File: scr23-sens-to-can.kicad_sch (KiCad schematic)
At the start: 67 parts, among them J1 ATM13-12PA-BM01, U1 LDL1117S50R, U2 LM358_DFN, U3 LM358_DFN, U4 TJA1042T-3, U5 AP7370-33Y-13, U6 LM358_DFN, U7 LM358_DFN, U8 STM32G431CBT6, Y1 Crystal 4-48MHz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

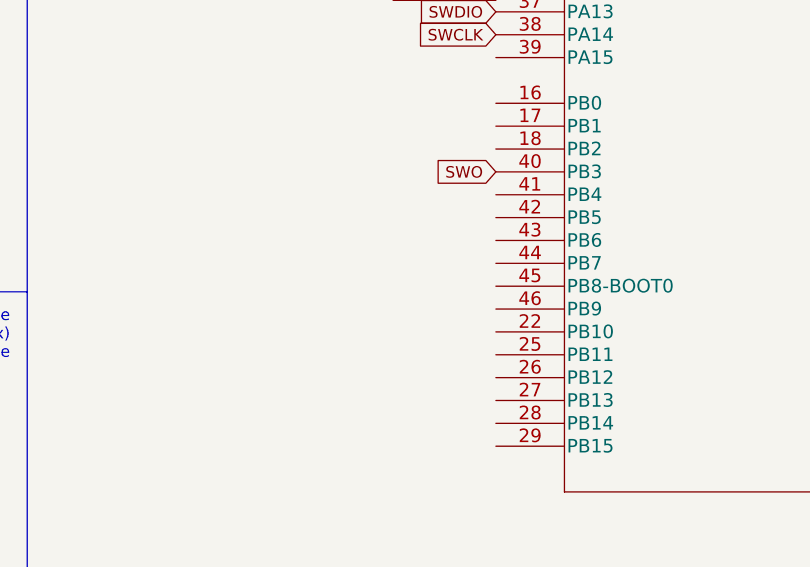
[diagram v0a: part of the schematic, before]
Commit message: added boot0 spdt
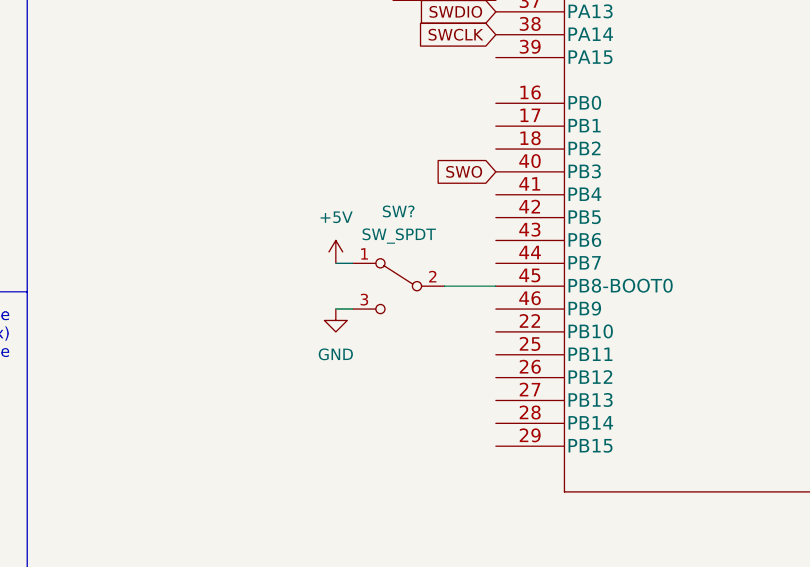
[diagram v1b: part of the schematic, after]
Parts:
- added SW?: SW_SPDT, symbol Switch:SW_SPDT
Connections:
- net +5V: now also SW?.1 (A)
- net GND: now also SW?.3 (C)
- net at U8.45 (PB8-BOOT0): now also SW?.2 (B)
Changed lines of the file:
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@@
     (stroke (width 0) (type default) (color 0 0 0 0))
   )
+  (wire (pts (xy 256.54 97.79) (xy 262.255 97.79))
+    (stroke (width 0) (type default) (color 0 0 0 0))
+  )
   (wire (pts (xy 364.49 39.37) (xy 364.49 36.195))
     (stroke (width 0) (type default) (color 0 0 0 0))
@@
     (stroke (width 0) (type default) (color 0 0 0 0))
   )
+  (wire (pts (xy 244.475 95.25) (xy 246.38 95.25))
+    (stroke (width 0) (type default) (color 0 0 0 0))
+  )
   (wire (pts (xy 57.785 127.635) (xy 54.61 127.635))
     (stroke (width 0) (type default) (color 0 0 0 0))
@@
     (stroke (width 0) (type default) (color 0 0 0 0))
   )
+  (wire (pts (xy 244.475 100.33) (xy 246.38 100.33))
+    (stroke (width 0) (type default) (color 0 0 0 0))
+  )
   (wire (pts (xy 154.94 39.37) (xy 165.1 39.37))
     (stroke (width 0) (type default) (color 0 0 0 0))
@@
     (pin "1")
   )
+  (symbol (lib_id "Switch:SW_SPDT") (at 251.46 97.79 0) (mirror y) (unit 1)
+    (in_bom yes) (on_board yes) (fields_autoplaced)
+    (property "Reference" "SW?" (id 0) (at 251.46 89.535 0))
+    (property "Value" "SW_SPDT" (id 1) (at 251.46 92.075 0))
+    (property "Footprint" "" (id 2) (at 251.46 97.79 0)
+      (effects (font (size 1.27 1.27)) hide)
+    )
+    (property "Datasheet" "~" (id 3) (at 251.46 97.79 0)
+      (effects (font (size 1.27 1.27)) hide)
+    )
+    (pin "1")
+    (pin "2")
+    (pin "3")
+  )
   (symbol (lib_id "Amplifier_Operational:LM358_DFN") (at 186.69 169.545 0) (unit 1)
     (in_bom yes) (on_board yes) (fields_autoplaced)
@@
     (pin "2")
   )
+  (symbol (lib_id "power:+5V") (at 244.475 95.25 0) (unit 1)
+    (in_bom yes) (on_board yes) (fields_autoplaced)
+    (property "Reference" "#PWR?" (id 0) (at 244.475 99.06 0)
+      (effects (font (size 1.27 1.27)) hide)
+    )
+    (property "Value" "+5V" (id 1) (at 244.475 90.17 0))
+    (property "Footprint" "" (id 2) (at 244.475 95.25 0)
+      (effects (font (size 1.27 1.27)) hide)
+    )
+    (property "Datasheet" "" (id 3) (at 244.475 95.25 0)
+      (effects (font (size 1.27 1.27)) hide)
+    )
+    (pin "1")
+  )
   (symbol (lib_id "scr23-sens-to-can-main:LDL1117S50R") (at 127.635 74.93 0) (unit 1)
     (in_bom yes) (on_board yes) (fields_autoplaced)
@@
     (pin "1")
   )
+  (symbol (lib_id "power:GND") (at 244.475 100.33 0) (unit 1)
+    (in_bom yes) (on_board yes) (fields_autoplaced)
+    (property "Reference" "#PWR?" (id 0) (at 244.475 106.68 0)
+      (effects (font (size 1.27 1.27)) hide)
+    )
+    (property "Value" "GND" (id 1) (at 244.475 105.41 0))
+    (property "Footprint" "" (id 2) (at 244.475 100.33 0)
+      (effects (font (size 1.27 1.27)) hide)
+    )
+    (property "Datasheet" "" (id 3) (at 244.475 100.33 0)
+      (effects (font (size 1.27 1.27)) hide)
+    )
+    (pin "1")
+  )
   (symbol (lib_id "power:+3.3V") (at 114.3 122.555 0) (unit 1)
     (in_bom yes) (on_board yes) (fields_autoplaced)
@@
       (reference "#PWR050") (unit 1) (value "GND") (footprint "")
     )
+    (path "/b2bb01a9-b60a-4528-aafa-2c7963462d4c"
+      (reference "#PWR?") (unit 1) (value "+5V") (footprint "")
+    )
+    (path "/cf8dda6e-a56a-43d8-94fc-1ec0cec4f2bf"
+      (reference "#PWR?") (unit 1) (value "GND") (footprint "")
+    )
     (path "/d8e70cec-745e-46da-bcc4-460dc4f54f47"
       (reference "C1") (unit 1) (value "10uF") (footprint "")
@@
       (reference "R18") (unit 1) (value "2670") (footprint "")
     )
+    (path "/098c6e6c-eb58-4a2a-b1cd-84ff9a7d7a07"
+      (reference "SW?") (unit 1) (value "SW_SPDT") (footprint "")
+    )
     (path "/b44bb0d9-577b-4e0b-a8dd-da899da62349"

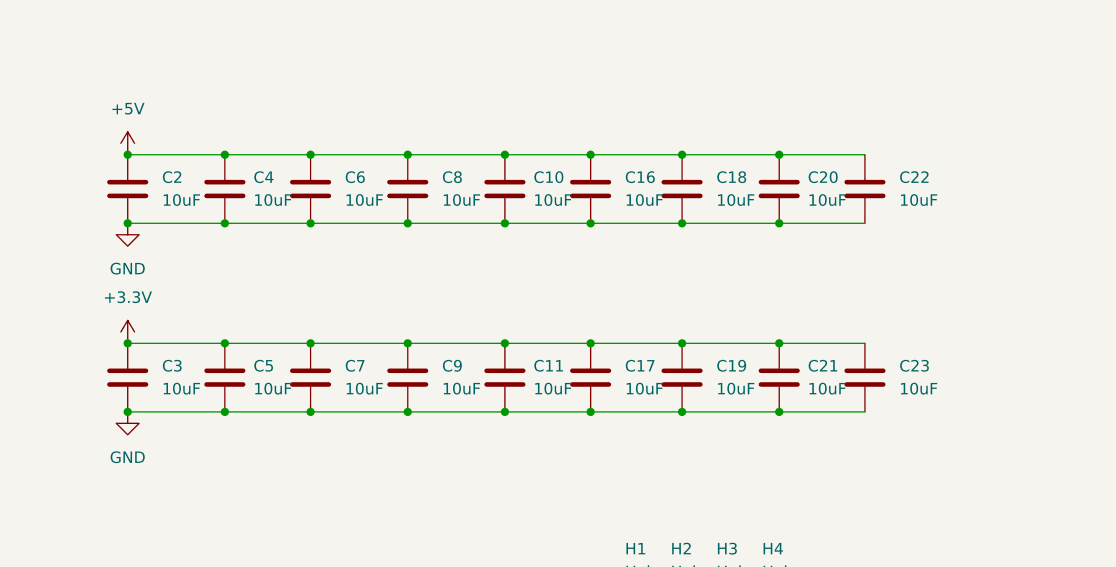
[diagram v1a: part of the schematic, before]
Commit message: change decoupling caps
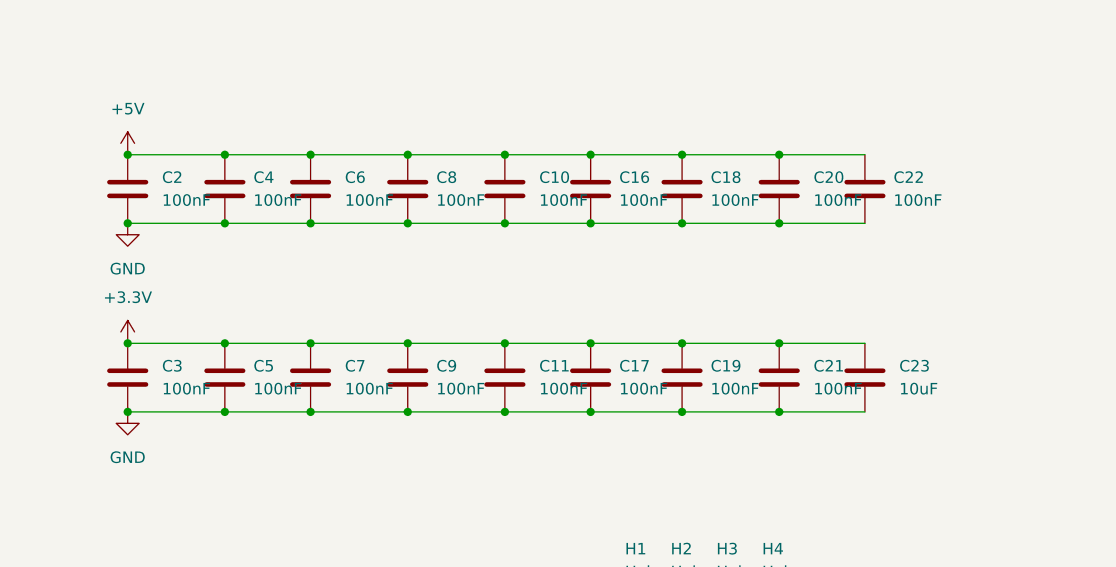
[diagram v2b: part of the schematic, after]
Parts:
- C10, C11, C16, C17, C18, C19, C2, C20, C21, C22, C3, C4, C5, C6, C7, C8, C9: value 10uF -> 100nF

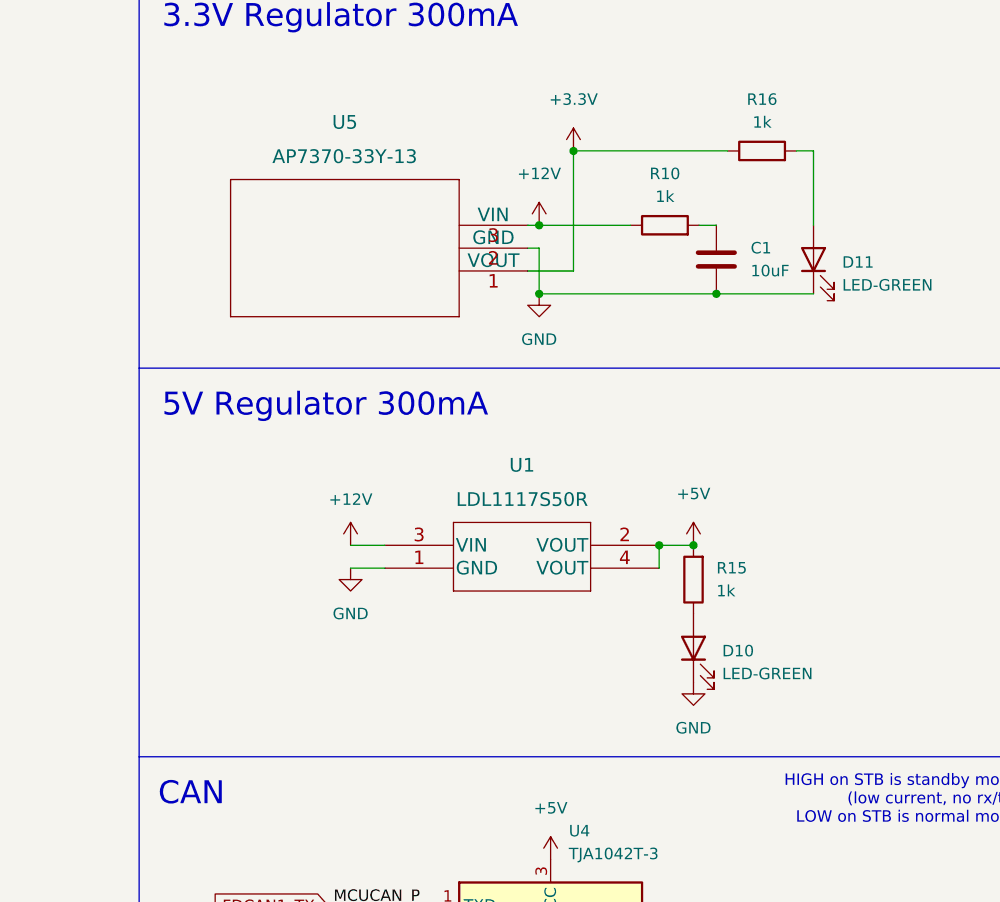
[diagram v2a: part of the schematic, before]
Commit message: change caps on 5v reg and put 5v/3.3v regulators in series
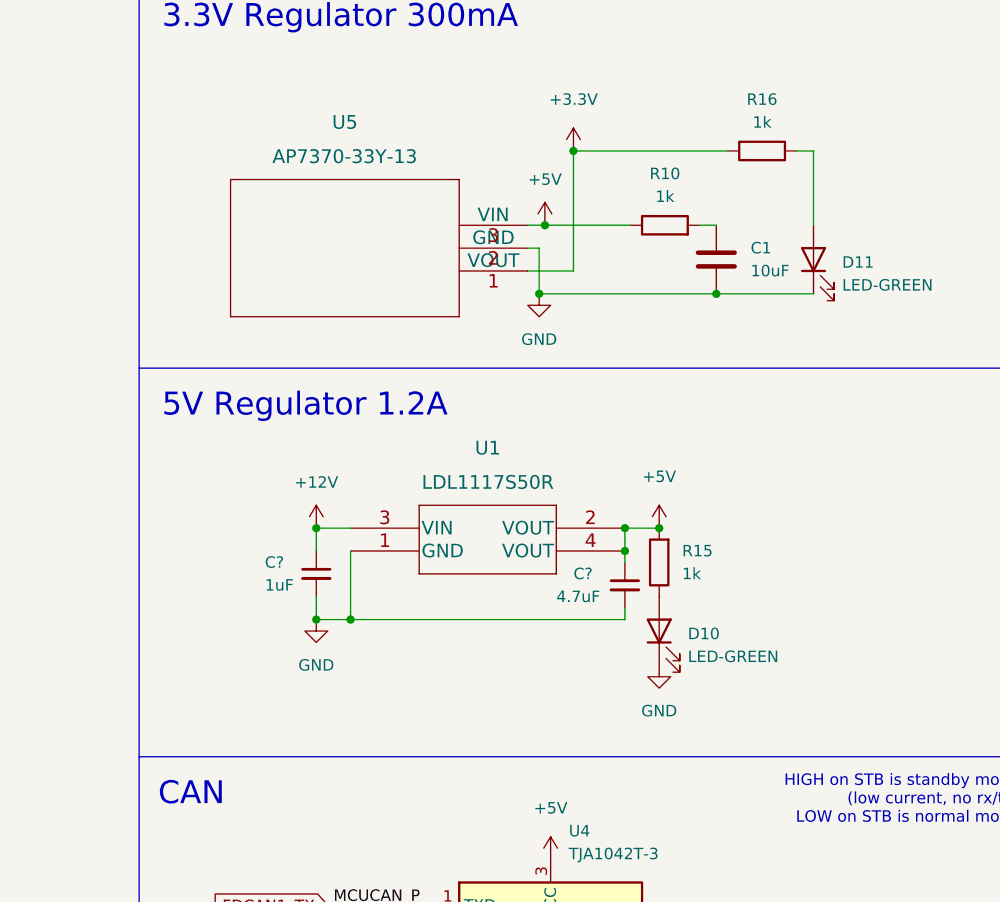
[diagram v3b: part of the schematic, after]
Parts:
- added C?: 1uF, symbol Device:C_Small
- added C?: 4.7uF, symbol Device:C_Small
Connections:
- net +12V: now also C?.1; no longer R10.1, U5.3 (VIN)
- net +5V: now also R10.1, U5.3 (VIN), C?.1
- net GND: now also C?.2, C?.2
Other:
- note added: "5V Regulator 1.2A"
- note removed: "5V Regulator 300mA"
- moved on the sheet: D10, R15, U1

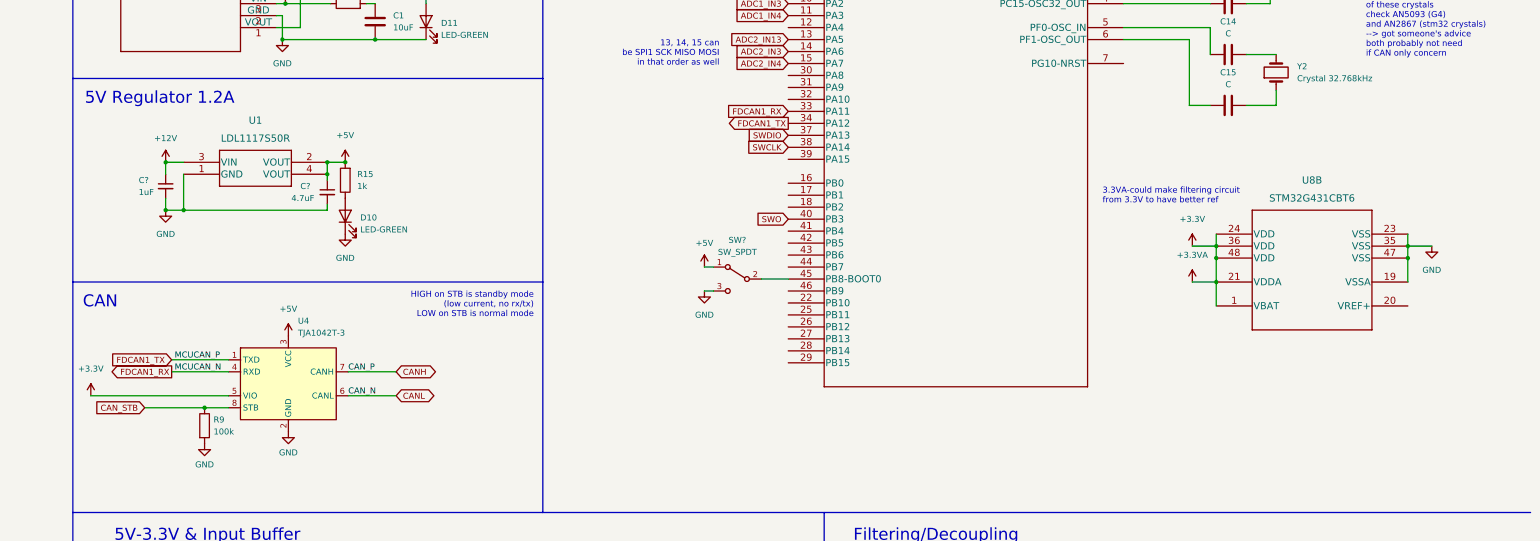
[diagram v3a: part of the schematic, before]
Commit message: switch to smps, add uC power supply filtering
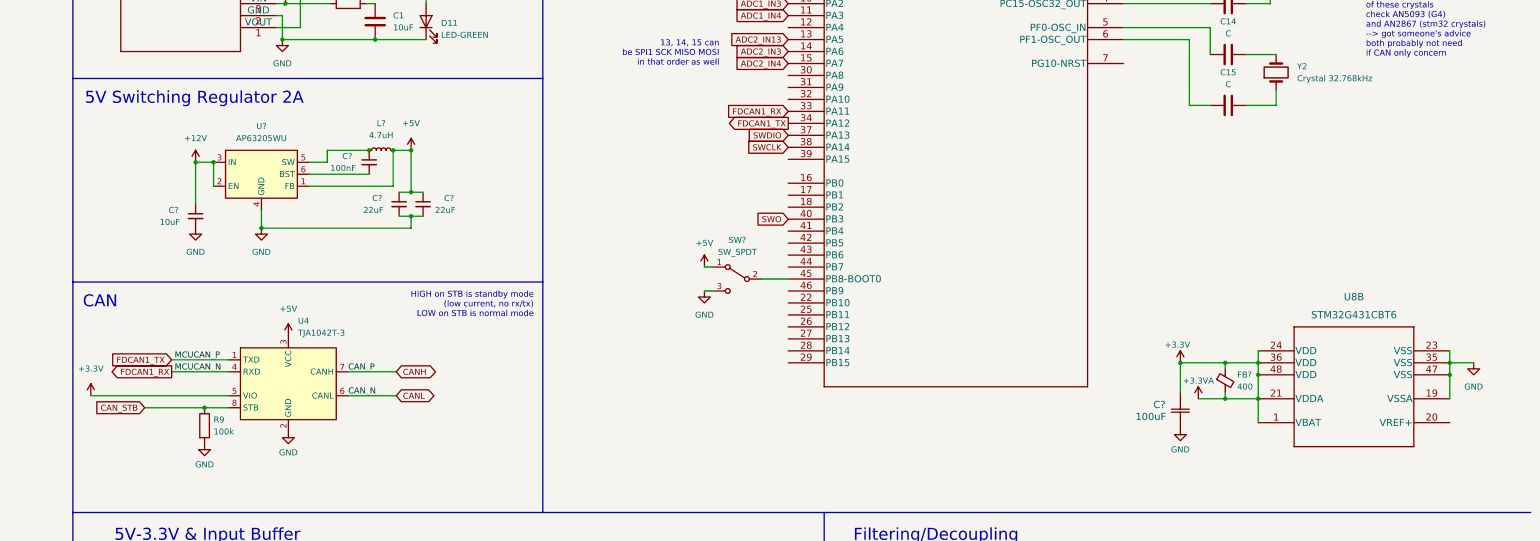
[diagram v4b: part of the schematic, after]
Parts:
- removed C?: 1uF, symbol Device:C_Small
- removed C?: 4.7uF, symbol Device:C_Small
- removed D10: LED-GREEN, symbol Device:LED
- removed R15: 1k, symbol Device:R
- removed U1: LDL1117S50R, SOT223_STM, symbol scr23-sens-to-can-main:LDL1117S50R
- added C?: 100nF, symbol Device:C_Small
- added C?: 100uF, TCJA_AVX, symbol scr23-sens-to-can-main:TCJA107M004R0200
- added C? (x2): 22uF, symbol Device:C_Small
- added C?: 10uF, symbol Device:C_Small
- added FB?: 400, symbol Device:FerriteBead_Small
- added L?: 4.7uH, symbol Device:L_Small
- added U?: AP63205WU, Package_TO_SOT_SMD:TSOT-23-6, symbol Regulator_Switching:AP63205WU
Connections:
- net +12V: now also C?.1, U?.2 (EN), U?.3 (IN)
- net +3.3V: now also C?.1, FB?.1, FB?.2
- net +5V: now also C?.1, C?.1, L?.2, U?.1 (FB)
- net GND: now also C?.2, C?.2, C?.2, C?.2, U?.4 (GND)
- new net: C?.1, L?.1, U?.5 (SW)
- new net: C?.2, U?.6 (BST)
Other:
- note added: "5V Switching Regulator 2A"
- note removed: "3.3VA-could make filtering circuit from 3.3V to have better ref"
- note removed: "5V Regulator 1.2A"
- moved on the sheet: U8B

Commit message: add notes
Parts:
- removed D1, D3, D4, D5, D6, D7, D8, D9: D_TVS, symbol Device:D_TVS
- added D?: LED-GREEN, symbol Device:LED
- added R?: 1k, symbol Device:R
- added U? (x2): SRV05-4, Package_TO_SOT_SMD:SOT-23-6, symbol Power_Protection:SRV05-4
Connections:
- net +5V: now also R?.1, U?.5 (VP), U?.5 (VP)
- net A0: now also U?.1 (IO1)
- net A1: now also U?.3 (IO2)
- net A2: now also U?.4 (IO3)
- net A3: now also U?.6 (IO4)
- net A4: now also U?.1 (IO1)
- net A5: now also U?.3 (IO2)
- net A6: now also U?.4 (IO3)
- net GND: now also D?.1 (K), U?.2 (VN), U?.2 (VN)
- new net: D?.2 (A), R?.2
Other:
- note added: "3.3V LDO 300mA"
- note added: "5V-3.3V Input Buffer"
- note added: "Extra Filtering/Decoupling"
- note removed: "3.3V Regulator 300mA"
- note removed: "5V-3.3V & Input Buffer"
- note removed: "Filtering/Decoupling"
- moved on the sheet: D2, J1

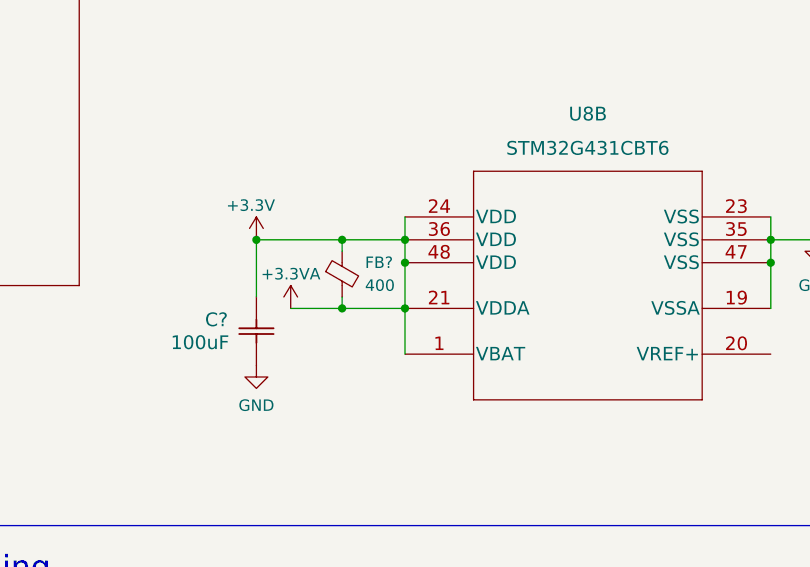
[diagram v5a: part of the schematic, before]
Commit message: add tantalum decoupling cap to stm32 power rail
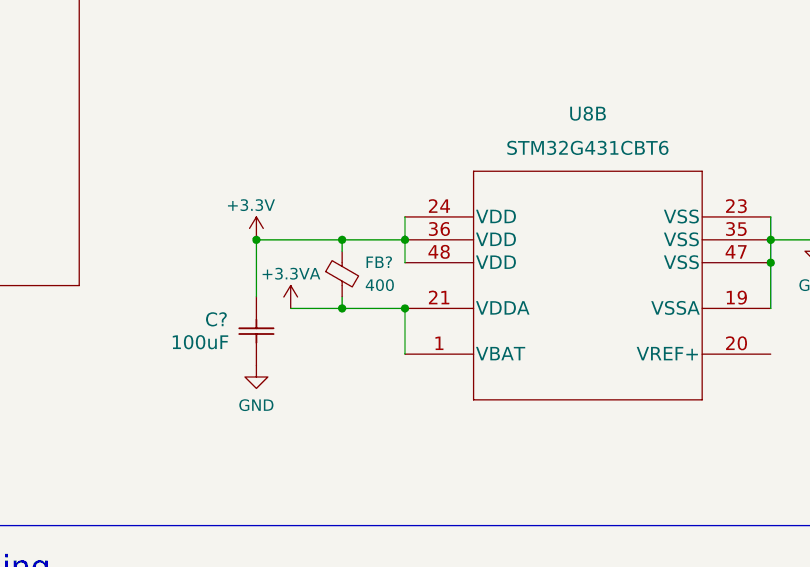
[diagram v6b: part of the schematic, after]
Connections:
- net +3.3V: no longer FB?.2, U8.1 (VBAT), U8.21 (VDDA)
- new net +3.3VA: FB?.2, U8.1 (VBAT), U8.21 (VDDA)
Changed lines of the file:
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@@
   (junction (at 330.2 196.215) (diameter 0) (color 0 0 0 0)
   )
-  (junction (at 361.95 118.11) (diameter 0) (color 0 0 0 0)
-  )
   (junction (at 361.315 182.88) (diameter 0) (color 0 0 0 0)
   )
@@
   )
   (wire (pts (xy 182.245 84.455) (xy 184.785 84.455))
-    (stroke (width 0) (type default) (color 0 0 0 0))
-  )
-  (wire (pts (xy 361.95 118.11) (xy 361.95 123.19))
     (stroke (width 0) (type default) (color 0 0 0 0))
   )
@@
   )
   (text "13, 14, 15 can \nbe SPI1 SCK MISO MOSI\nin that order as well"
-    (at 247.65 52.705 180)
+    (at 247.65 52.705 0)
     (effects (font (size 1.27 1.27)) (justify right bottom))
   )
@@
   )
   (text "HIGH on STB is standby mode\n(low current, no rx/tx)\nLOW on STB is normal mode"
-    (at 208.28 106.045 180)
+    (at 208.28 106.045 0)
     (effects (font (size 1.27 1.27)) (justify right bottom))
   )
@@
       (effects (font (size 1.524 1.524)) hide)
     )
-    (property "Datasheet" "" (id 3) (at 345.44 121.92 0)
-      (effects (font (size 1.524 1.524)))
-    )
-    (pin "1")
+    (property "Datasheet" "https://datasheets.kyocera-avx.com/TCJ.pdf" (id 3) (at 345.44 121.92 0)
+      (effects (font (size 1.524 1.524)) hide)
+    )
+    (pin "1")

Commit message: spec smps inductor, might want to go 6.8uH with ~2.5A according to equations...but went 2A 4.7uH :)
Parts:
- L?: footprint (none) -> Inductor_SMD:L_Bourns-SRN4018
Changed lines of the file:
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@@
     (property "Reference" "L?" (id 0) (at 175.895 64.77 90))
     (property "Value" "4.7uH" (id 1) (at 175.895 67.31 90))
-    (property "Footprint" "" (id 2) (at 175.895 70.485 0)
-      (effects (font (size 1.27 1.27)) hide)
-    )
-    (property "Datasheet" "~" (id 3) (at 175.895 70.485 0)
+    (property "Footprint" "Inductor_SMD:L_Bourns-SRN4018" (id 2) (at 175.895 70.485 0)
+      (effects (font (size 1.27 1.27)) hide)
+    )
+    (property "Datasheet" "https://www.mouser.com/datasheet/2/54/srn4018-1391320.pdf" (id 3) (at 175.895 70.485 0)
       (effects (font (size 1.27 1.27)) hide)
     )
@@
     )
     (path "/64d56d94-2bd1-45bd-8c62-6e7a6aff5745"
-      (reference "L?") (unit 1) (value "4.7uH") (footprint "")
+      (reference "L?") (unit 1) (value "4.7uH") (footprint "Inductor_SMD:L_Bourns-SRN4018")
     )
     (path "/26448f24-3374-419d-a536-be915a2394ea"
